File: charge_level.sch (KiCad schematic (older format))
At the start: 34 parts

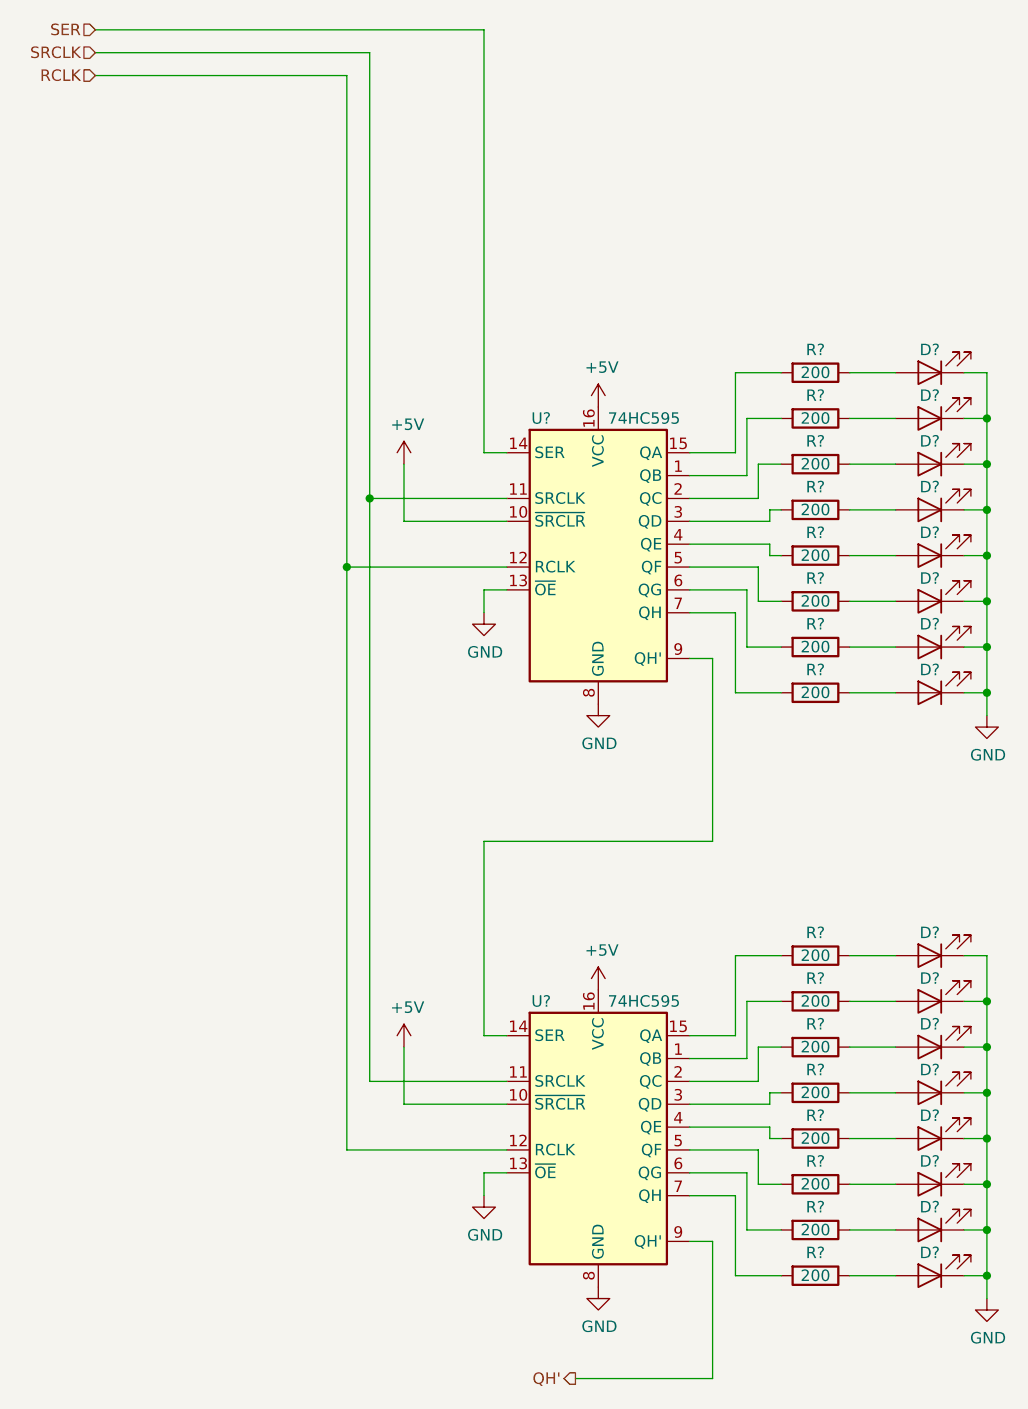
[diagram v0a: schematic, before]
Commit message: footprints; library for 7seg; start pcb layout
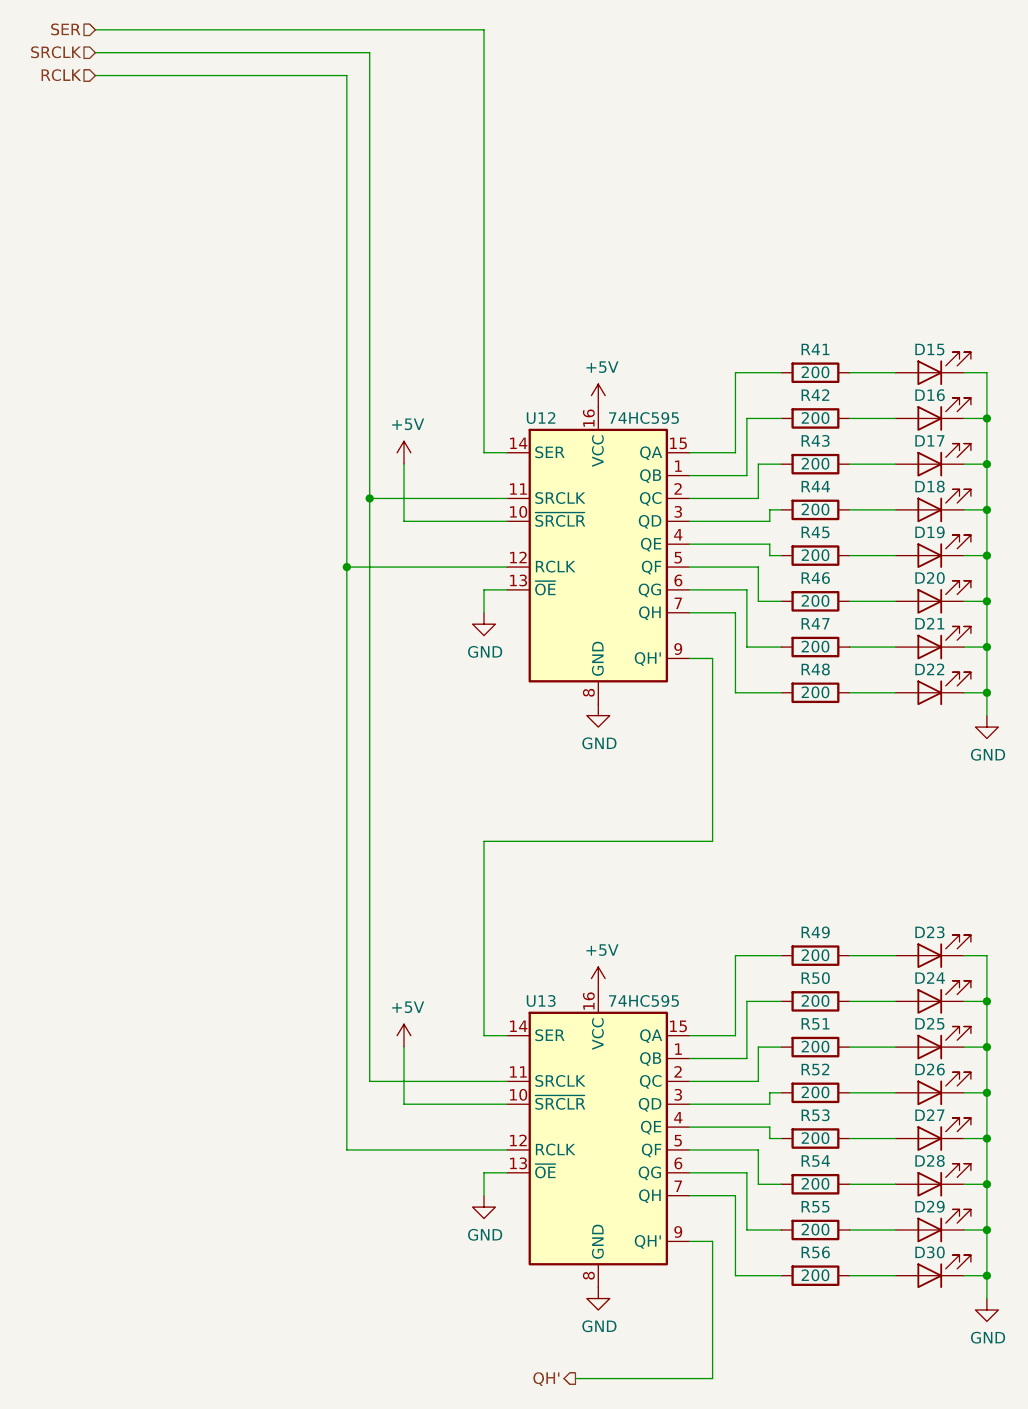
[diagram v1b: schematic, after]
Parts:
- D15, D16, D17, D18, D19, D20, D21, D22, D23, D24, D25, D26, D27, D28, D29, D30: renamed from D?; footprint (none) -> LED_THT:LED_D3.0mm_Clear
- R41, R42, R43, R44, R45, R46, R47, R48, R49, R50, R51, R52, R53, R54, R55, R56: renamed from R?; footprint (none) -> Resistor_SMD:R_0603_1608Metric
- U12, U13: renamed from U?; footprint (none) -> Package_SO:SOIC-16_3.9x9.9mm_P1.27mm
